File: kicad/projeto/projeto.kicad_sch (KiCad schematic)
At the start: 4 parts

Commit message: Iniciou o esquemático
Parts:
- removed Q?: BTA16-600B, Package_TO_SOT_THT:TO-220-3_Vertical, symbol Triac_Thyristor:BTA16-600B
- removed R? (x2): R, symbol Device:R
- removed Vca: VSIN, symbol Simulation_SPICE:VSIN
- added D01, D02, D03, D04, D?: UF5408, Diode_THT:D_DO-201AD_P15.24mm_Horizontal, symbol Diode:UF5408
- added D05: 5V, symbol Device:D_Zener
- added D?, Dss: LED, LED_THT:LED_D3.0mm, symbol Device:LED
- added J?: Conn_01x02_Male, Connector_PinHeader_2.54mm:PinHeader_1x02_P2.54mm_Vertical, symbol Connector:Conn_01x02_Male
- added Jac, Jl1, Jl2: Screw_Terminal_01x02, TerminalBlock:TerminalBlock_bornier-2_P5.08mm, symbol Connector:Screw_Terminal_01x02
- added Jdc: Barrel_Jack_MountingPin, Connector_BarrelJack:BarrelJack_Horizontal, symbol Connector:Barrel_Jack_MountingPin
- added Jsens: Screw_Terminal_01x06, TerminalBlock:TerminalBlock_bornier-6_P5.08mm, symbol Connector:Screw_Terminal_01x06
- added Q1, Q2: BTA16-600B, Package_TO_SOT_THT:TO-220-3_Vertical, symbol Triac_Thyristor:BTA16-600B
- added R01: 33k, Resistor_THT:R_Axial_DIN0207_L6.3mm_D2.5mm_P7.62mm_Horizontal, symbol Device:R
- added R02, Ren, Rexit, Rreset, Rsens1, Rsens2: 33K, Resistor_THT:R_Axial_DIN0207_L6.3mm_D2.5mm_P7.62mm_Horizontal, symbol Device:R
- added R?: R, Resistor_THT:R_Axial_DIN0207_L6.3mm_D2.5mm_P7.62mm_Horizontal, symbol Device:R
- added Rmoc1, Rmoc2: 150, Resistor_THT:R_Axial_DIN0207_L6.3mm_D2.5mm_P7.62mm_Horizontal, symbol Device:R
- added Rss: 260, Resistor_THT:R_Axial_DIN0207_L6.3mm_D2.5mm_P7.62mm_Horizontal, symbol Device:R
- added Rtriac1, Rtriac2: 180, Resistor_THT:R_Axial_DIN0309_L9.0mm_D3.2mm_P12.70mm_Horizontal, symbol Device:R
- added SWexit, SWreset: SW_Push, symbol Switch:SW_Push
- added U?: LM1117-3.3, symbol Regulator_Linear:LM1117-3.3
- added U?: ESP-12E, RF_Module:ESP-12E, symbol RF_Module:ESP-12E
- added Udet_0: 4N25, Package_DIP:DIP-6_W7.62mm, symbol Isolator:4N25
- added Uload1, Uload2: MOC3021M, symbol Relay_SolidState:MOC3021M
- added Umultiplex: CD4051B, Package_DIP:DIP-16_W7.62mm, symbol Analog_Switch:CD4051B
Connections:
- net GND: now also Dss.1 (K), Jdc.2, Rexit.2, Rsens2.2, SWreset.2, U?.1 (GND), Udet_0.4, Uload1.2, Uload2.2, Umultiplex.2 (X6), Umultiplex.4 (X7), Umultiplex.6 (INH), Umultiplex.7 (VEE), Umultiplex.8 (VSS)
- new net: D01.1 (K), D03.1 (K), D05.1 (K)
- new net: Rtriac1.1, Uload1.6
- new net: Jl1.2 (Pin_2), Q1.2 (A2), Rtriac1.2
- new net: Rmoc1.1, Uload1.1
- new net: Q1.3 (G), Uload1.4
- new net: D02.2 (A), D04.2 (A), Udet_0.2
- new net: Dss.2 (A), Rss.2
- new net: R01.2, Udet_0.1
- new net: Ren.1, U?.3 (EN)
- new net: D05.2 (A), R01.1
- new net: Rtriac2.1, Uload2.6
- new net: Jl2.2 (Pin_2), Q2.2 (A2), Rtriac2.2
- new net: Jsens.5 (Pin_5), Umultiplex.1 (X4)
- new net: Jsens.4 (Pin_4), Umultiplex.12 (X3)
- new net: Jsens.1 (Pin_1), Umultiplex.13 (X0)
- new net: Jsens.2 (Pin_2), Umultiplex.14 (X1)
- new net: Jsens.3 (Pin_3), Umultiplex.15 (X2)
- new net: Rsens1.1, Umultiplex.3 (X)
- new net: Jsens.6 (Pin_6), Umultiplex.5 (X5)
- new net: Rmoc2.1, Uload2.1
- new net: Q2.3 (G), Uload2.4
- new net +3V3: R02.1, Ren.2, Rreset.1, SWexit.1, U?.2 (VO), Umultiplex.16 (VDD)
- new net +5V: Jdc.1, U?.3 (VI)
- new net AC1: D01.2 (A), D02.1 (K), Jac.1 (Pin_1), Jl1.1 (Pin_1), Jl2.1 (Pin_1)
- new net AC2: D03.2 (A), D04.1 (K), Jac.2 (Pin_2), Q1.1 (A1), Q2.1 (A1)
- new net NC?: Jdc.MP (MountPin), Udet_0.6
- new net det_0_intr: R02.2, Udet_0.5
- new net drive_load_1: Rmoc1.2
- new net drive_load_2: Rmoc2.2
- new net exit_intr: Rexit.1, SWexit.2
- new net multiplex_A: U?.4 (GPIO16), Umultiplex.11 (A)
- new net multiplex_B: U?.5 (GPIO14), Umultiplex.10 (B)
- new net multiplex_C: U?.6 (GPIO12), Umultiplex.9 (C)
- new net multiplex_out: Rsens1.2, Rsens2.1, U?.2 (ADC)
- new net reset: Rreset.2, SWreset.1, U?.1 (~{RST})
- new net steady_state: Rss.1
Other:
- note added: "Buttons"
- note added: "COLOCAR A CONEXÃO DO 5V VINDO DO SERIAL AQUI"
- note added: "Load Driver"
- note added: "Power"
- note added: "Sensor"
- note added: "Steady State Status"
- note added: "Zero Detection"
- note removed: ".include D:\bolsa\controle_forno\circuitos\lib\moc302x.lib"
- note removed: ".tran 1u 0.05"

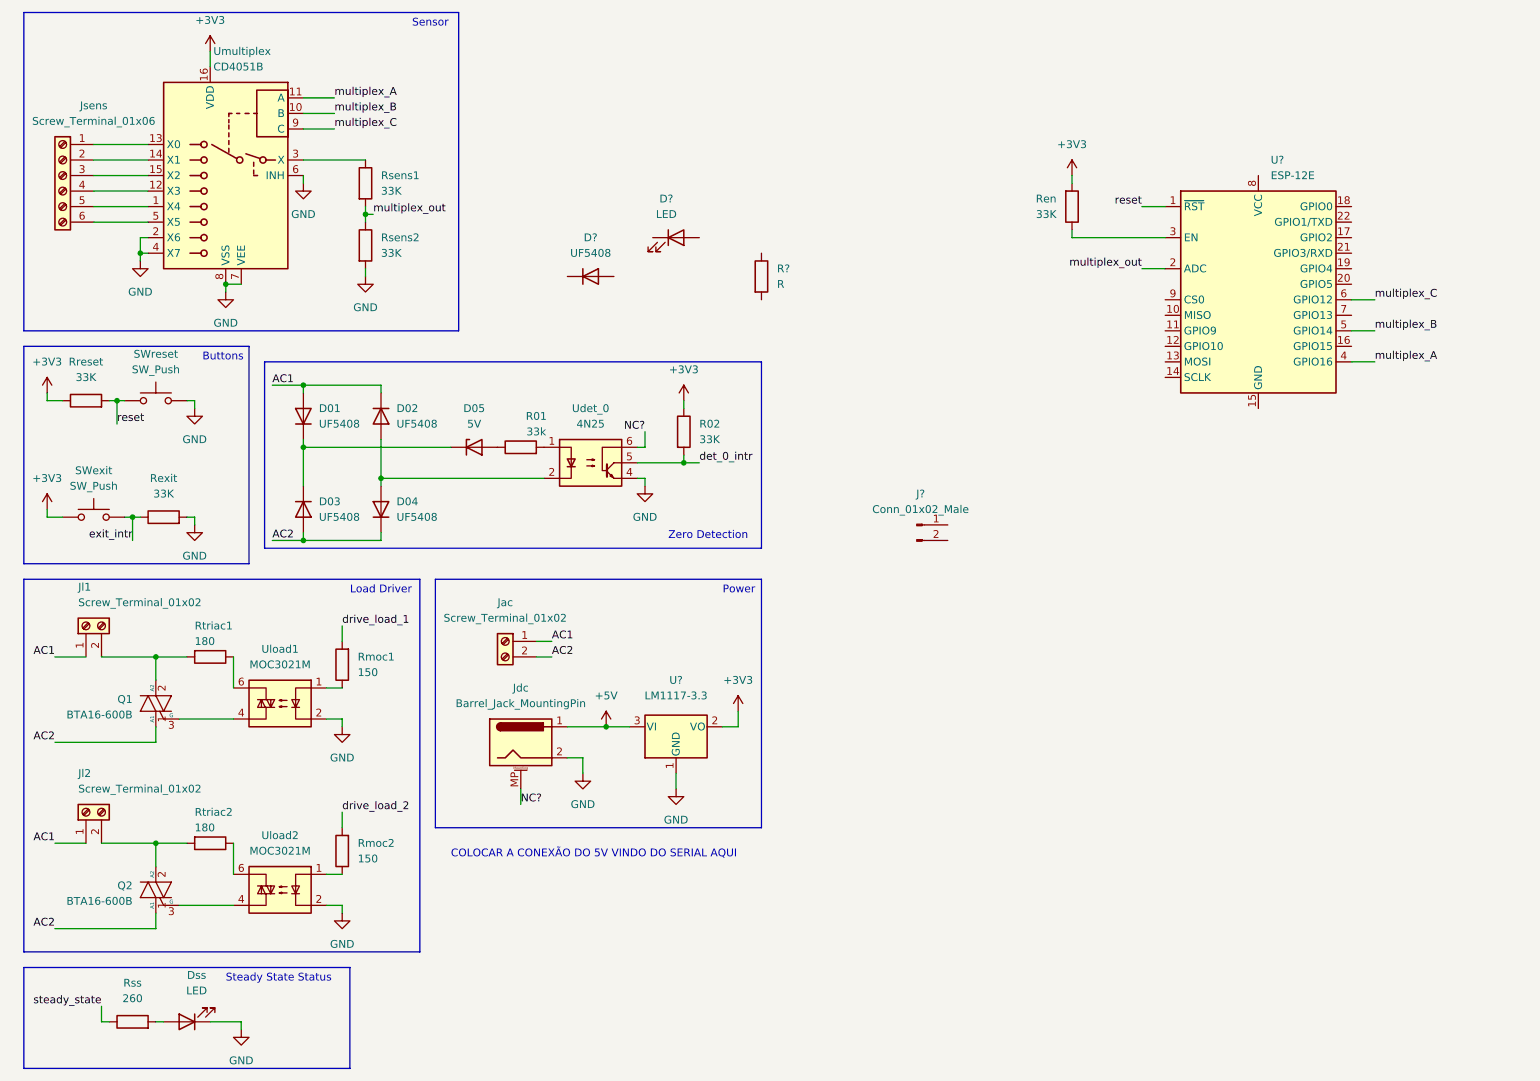
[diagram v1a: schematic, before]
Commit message: Finalizou esquematico
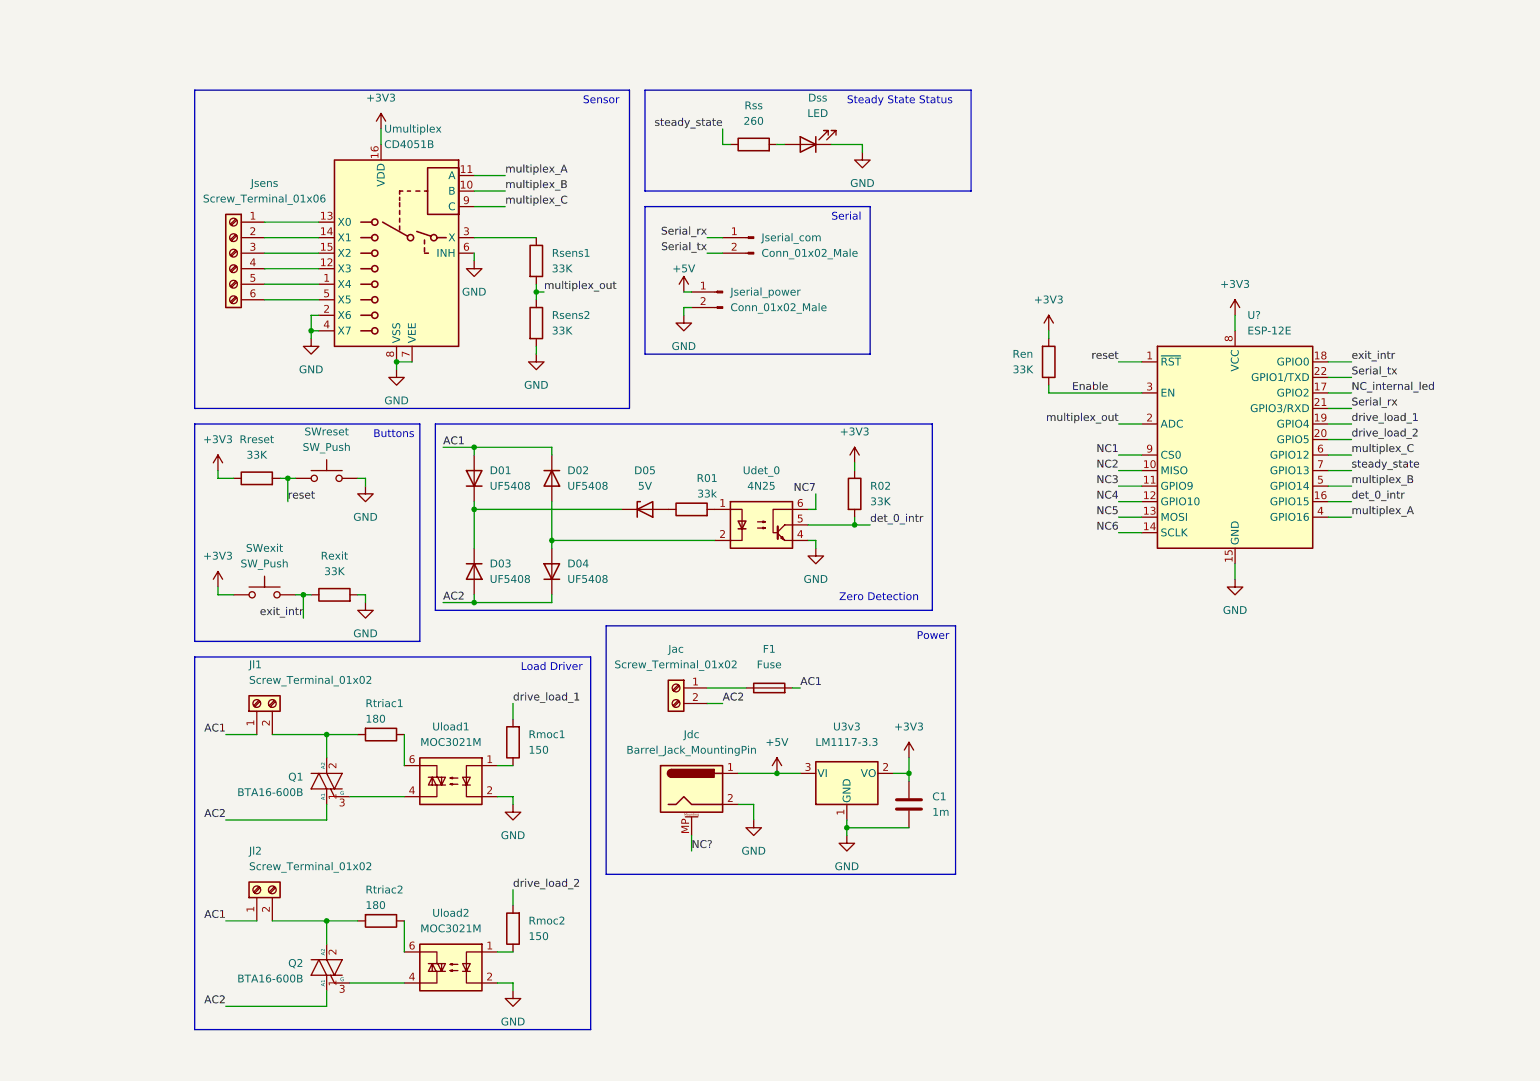
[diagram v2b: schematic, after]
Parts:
- removed D?: UF5408, Diode_THT:D_DO-201AD_P15.24mm_Horizontal, symbol Diode:UF5408
- removed D?: LED, LED_THT:LED_D3.0mm, symbol Device:LED
- removed J?: Conn_01x02_Male, Connector_PinHeader_2.54mm:PinHeader_1x02_P2.54mm_Vertical, symbol Connector:Conn_01x02_Male
- removed R?: R, Resistor_THT:R_Axial_DIN0207_L6.3mm_D2.5mm_P7.62mm_Horizontal, symbol Device:R
- added C1: 1m, symbol Device:C
- added F1: Fuse, Fuse:Fuseholder_Cylinder-5x20mm_Stelvio-Kontek_PTF78_Horizontal_Open, symbol Device:Fuse
- added Jserial_com, Jserial_power: Conn_01x02_Male, Connector_PinHeader_2.54mm:PinHeader_1x02_P2.54mm_Vertical, symbol Connector:Conn_01x02_Male
- U3v3: renamed from U?; footprint (none) -> Package_TO_SOT_THT:TO-220-3_Vertical
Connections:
- net +3V3: now also U?.8 (VCC), C1.1
- net +5V: now also Jserial_power.1 (Pin_1)
- net AC1: now also F1.2; no longer Jac.1 (Pin_1)
- net GND: now also U?.15 (GND), C1.2, Jserial_power.2 (Pin_2)
- net NC?: no longer Udet_0.6
- net det_0_intr: now also U?.16 (GPIO15)
- net drive_load_1: now also U?.19 (GPIO4)
- net drive_load_2: now also U?.20 (GPIO5)
- net exit_intr: now also U?.18 (GPIO0)
- net steady_state: now also U?.7 (GPIO13)
- net Enable: now reaches Ren.1, U?.3 (EN)
- net NC2: now reaches U?.10 (MISO)
- net NC3: now reaches U?.11 (GPIO9)
- net NC4: now reaches U?.12 (GPIO10)
- net NC5: now reaches U?.13 (MOSI)
- net NC6: now reaches U?.14 (SCLK)
- net NC_internal_led: now reaches U?.17 (GPIO2)
- net Serial_rx: now reaches U?.21 (GPIO3/RXD)
- net Serial_rx: now also Jserial_com.1 (Pin_1)
- net Serial_tx: now reaches U?.22 (GPIO1/TXD)
- net Serial_tx: now also Jserial_com.2 (Pin_2)
- net NC1: now reaches U?.9 (CS0)
- new net: F1.1, Jac.1 (Pin_1)
- new net NC7: Udet_0.6
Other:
- note added: "Serial"
- note removed: "COLOCAR A CONEXÃO DO 5V VINDO DO SERIAL AQUI"
- company: (none) -> LITel UFJF
- moved on the sheet: D01, D02, D03, D04, D05, Dss, Jac, Jdc, Jl1, Jl2, Jsens, Q1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

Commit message: Correção de erros do ERC
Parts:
- C1: footprint (none) -> Capacitor_THT:C_Radial_D10.0mm_H16.0mm_P5.00mm
- gave numbers to parts that had none: 1
- renumbered D01 to D1, D02 to D2, D03 to D3, D04 to D4, D05 to D5, Dss to Dss1, Jac to Jac1, Jdc to Jdc1, Jsens to Jsens1, Jserial_com to Jserial_com1, Jserial_power to Jserial_power1, R01 to R1, R02 to R2, Ren to Ren1, Rexit to Rexit1, Rreset to Rreset1, Rss to Rss1, SWexit to SWexit1, SWreset to SWreset1, Umultiplex to Umultiplex1
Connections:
- net GND: no longer Umultiplex1.2 (X6), Umultiplex1.4 (X7)
- net NC1: no longer names the net of U1.9 (CS0)
- net NC2: no longer names the net of U1.10 (MISO)
- net NC3: no longer names the net of U1.11 (GPIO9)
- net NC4: no longer names the net of U1.12 (GPIO10)
- net NC5: no longer names the net of U1.13 (MOSI)
- net NC6: no longer names the net of U1.14 (SCLK)
- net NC7: no longer names the net of Udet_0.6
- net NC?: no longer names the net of Jdc1.MP (MountPin)
- net NC_internal_led: no longer names the net of U1.17 (GPIO2)
- no-connect marks 0 -> 11
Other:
- note added: "NC_internal_led"
- moved on the sheet: C1, U3v3

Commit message: Att componentes
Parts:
- removed Jsens1: Screw_Terminal_01x06, TerminalBlock:TerminalBlock_bornier-6_P5.08mm, symbol Connector:Screw_Terminal_01x06
- added Jpwr_sens1, Jpwr_sens2, Jsens1: Conn_01x08_Male, Connector_PinHeader_2.54mm:PinHeader_1x08_P2.54mm_Vertical, symbol Connector:Conn_01x08_Male
- Rexit1, Rreset1, Rsens1, Rsens2: value 33K -> 10K
- Rmoc1, Rmoc2: value 150 -> 240
- Rz1: renamed from R1; footprint Resistor_THT:R_Axial_DIN0207_L6.3mm_D2.5mm_P7.62mm_Horizontal -> Resistor_THT:R_Axial_DIN0207_L6.3mm_D2.5mm_P10.16mm_Horizontal
- SWexit1, SWreset1: footprint (none) -> Button_Switch_THT:SW_PUSH_6mm
- Uload1, Uload2: value MOC3021M -> MOC3023M; footprint (none) -> Package_DIP:DIP-6_W7.62mm_Socket
- Umultiplex1: footprint Package_DIP:DIP-16_W7.62mm -> Package_DIP:DIP-16_W7.62mm_Socket
- renumbered R2 to Rz2
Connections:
- net +5V: now also Jpwr_sens1.1 (Pin_1), Jpwr_sens1.2 (Pin_2), Jpwr_sens1.3 (Pin_3), Jpwr_sens1.4 (Pin_4), Jpwr_sens1.5 (Pin_5), Jpwr_sens1.6 (Pin_6), Jpwr_sens1.7 (Pin_7), Jpwr_sens1.8 (Pin_8)
- net GND: now also Jpwr_sens2.1 (Pin_1), Jpwr_sens2.2 (Pin_2), Jpwr_sens2.3 (Pin_3), Jpwr_sens2.4 (Pin_4), Jpwr_sens2.5 (Pin_5), Jpwr_sens2.6 (Pin_6), Jpwr_sens2.7 (Pin_7), Jpwr_sens2.8 (Pin_8)
- net at Umultiplex1.1 (X4): now also Jsens1.5 (Pin_5)
- net at Umultiplex1.12 (X3): now also Jsens1.4 (Pin_4)
- net at Umultiplex1.13 (X0): now also Jsens1.1 (Pin_1)
- net at Umultiplex1.14 (X1): now also Jsens1.2 (Pin_2)
- net at Umultiplex1.15 (X2): now also Jsens1.3 (Pin_3)
- net at Umultiplex1.2 (X6): now also Jsens1.7 (Pin_7)
- net at Umultiplex1.4 (X7): now also Jsens1.8 (Pin_8)
- net at Umultiplex1.5 (X5): now also Jsens1.6 (Pin_6)
- no-connect marks 11 -> 9
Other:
- moved on the sheet: Ren1, U1

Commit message: Att componentes
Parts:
- added C1: 1m, Capacitor_THT:C_Radial_D10.0mm_H16.0mm_P5.00mm, symbol Device:C
- renumbered C1 to C2
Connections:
- net +5V: now also C1.1
- net GND: now also C1.2
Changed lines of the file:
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@@
   (junction (at 60.96 110.49) (diameter 0) (color 0 0 0 0)
   )
-  (junction (at 134.62 144.78) (diameter 0) (color 0 0 0 0)
-  )
   (junction (at 210.82 138.43) (diameter 0) (color 0 0 0 0)
   )
@@
   (junction (at 199.39 133.35) (diameter 0) (color 0 0 0 0)
   )
+  (junction (at 138.43 147.32) (diameter 0) (color 0 0 0 0)
+  )
   (junction (at 58.42 91.44) (diameter 0) (color 0 0 0 0)
   )
@@
   )
   (junction (at 64.77 133.35) (diameter 0) (color 0 0 0 0)
+  )
+  (junction (at 134.62 147.32) (diameter 0) (color 0 0 0 0)
+  )
+  (junction (at 138.43 139.7) (diameter 0) (color 0 0 0 0)
   )
   (junction (at 152.4 139.7) (diameter 0) (color 0 0 0 0)
@@
   (no_connect (at 144.78 96.52))
   (no_connect (at 241.3 58.42))
+  (wire (pts (xy 165.1 148.59) (xy 175.26 148.59))
+    (stroke (width 0) (type default) (color 0 0 0 0))
+  )
   (wire (pts (xy 64.77 144.78) (xy 64.77 147.32))
     (stroke (width 0) (type default) (color 0 0 0 0))
@@
     (stroke (width 0) (type default) (color 0 0 0 0))
   )
+  (wire (pts (xy 138.43 139.7) (xy 152.4 139.7))
+    (stroke (width 0) (type default) (color 0 0 0 0))
+  )
   (wire (pts (xy 127 52.07) (xy 129.54 52.07))
     (stroke (width 0) (type default) (color 0 0 0 0))
@@
     (stroke (width 0) (type default) (color 0 0 0 0))
   )
+  (wire (pts (xy 134.62 147.32) (xy 138.43 147.32))
+    (stroke (width 0) (type default) (color 0 0 0 0))
+  )
   (wire (pts (xy 207.01 73.66) (xy 203.2 73.66))
     (stroke (width 0) (type default) (color 0 0 0 0))
@@
     (stroke (width 0) (type default) (color 0 0 0 0))
   )
-  (wire (pts (xy 132.08 139.7) (xy 152.4 139.7))
+  (wire (pts (xy 132.08 139.7) (xy 138.43 139.7))
     (stroke (width 0) (type default) (color 0 0 0 0))
   )
@@
   )
   (wire (pts (xy 140.97 125.73) (xy 142.24 125.73))
-    (stroke (width 0) (type default) (color 0 0 0 0))
-  )
-  (wire (pts (xy 165.1 148.59) (xy 175.26 148.59))
     (stroke (width 0) (type default) (color 0 0 0 0))
   )
@@
   )
   (symbol (lib_id "power:GND") (at 134.62 147.32 0) (unit 1)
-    (in_bom yes) (on_board yes) (fields_autoplaced)
+    (in_bom yes) (on_board yes)
     (property "Reference" "#PWR0108" (id 0) (at 134.62 153.67 0)
       (effects (font (size 1.27 1.27)) hide)
     )
-    (property "Value" "GND" (id 1) (at 134.62 152.4 0))
+    (property "Value" "GND" (id 1) (at 132.08 151.13 0))
     (property "Footprint" "" (id 2) (at 134.62 147.32 0)
       (effects (font (size 1.27 1.27)) hide)
@@
     )
     (property "Datasheet" "~" (id 3) (at 73.66 163.83 0)
+      (effects (font (size 1.27 1.27)) hide)
+    )
+    (pin "1")
+    (pin "2")
+  )
+  (symbol (lib_id "Device:C") (at 138.43 143.51 0) (unit 1)
+    (in_bom yes) (on_board yes) (fields_autoplaced)
+    (property "Reference" "C1" (id 0) (at 142.24 142.2399 0)
+      (effects (font (size 1.27 1.27)) (justify left))
+    )
+    (property "Value" "1m" (id 1) (at 142.24 144.7799 0)
+      (effects (font (size 1.27 1.27)) (justify left))
+    )
+    (property "Footprint" "Capacitor_THT:C_Radial_D10.0mm_H16.0mm_P5.00mm" (id 2) (at 139.3952 147.32 0)
+      (effects (font (size 1.27 1.27)) hide)
+    )
+    (property "Datasheet" "~" (id 3) (at 138.43 143.51 0)
       (effects (font (size 1.27 1.27)) hide)
     )
@@
   (symbol (lib_id "Device:C") (at 175.26 144.78 0) (unit 1)
     (in_bom yes) (on_board yes) (fields_autoplaced)
-    (property "Reference" "C1" (id 0) (at 179.07 143.5099 0)
+    (property "Reference" "C2" (id 0) (at 179.07 143.5099 0)
       (effects (font (size 1.27 1.27)) (justify left))
     )
@@
     (pin "2")
   )
-  (symbol (lib_id "power:PWR_FLAG") (at 134.62 144.78 0) (unit 1)
-    (in_bom yes) (on_board yes) (fields_autoplaced)
-    (property "Reference" "#FLG0101" (id 0) (at 134.62 142.875 0)
-      (effects (font (size 1.27 1.27)) hide)
-    )
-    (property "Value" "PWR_FLAG" (id 1) (at 137.16 143.5099 0)
-      (effects (font (size 1.27 1.27)) (justify left))
-    )
-    (property "Footprint" "" (id 2) (at 134.62 144.78 0)
-      (effects (font (size 1.27 1.27)) hide)
-    )
-    (property "Datasheet" "~" (id 3) (at 134.62 144.78 0)
+  (symbol (lib_id "power:PWR_FLAG") (at 138.43 147.32 180) (unit 1)
+    (in_bom yes) (on_board yes)
+    (property "Reference" "#FLG0101" (id 0) (at 138.43 149.225 0)
+      (effects (font (size 1.27 1.27)) hide)
+    )
+    (property "Value" "PWR_FLAG" (id 1) (at 147.32 151.13 0)
+      (effects (font (size 1.27 1.27)) (justify left))
+    )
+    (property "Footprint" "" (id 2) (at 138.43 147.32 0)
+      (effects (font (size 1.27 1.27)) hide)
+    )
+    (property "Datasheet" "~" (id 3) (at 138.43 147.32 0)
       (effects (font (size 1.27 1.27)) hide)
     )
@@
       (reference "#PWR0124") (unit 1) (value "GND") (footprint "")
     )
+    (path "/80ebf0af-a71f-42a9-abab-839fb7cffa2d"
+      (reference "C1") (unit 1) (value "1m") (footprint "Capacitor_THT:C_Radial_D10.0mm_H16.0mm_P5.00mm")
+    )
     (path "/da3a6a44-7c4e-4b57-b3f7-f3c72ed95869"
-      (reference "C1") (unit 1) (value "1m") (footprint "Capacitor_THT:C_Radial_D10.0mm_H16.0mm_P5.00mm")
+      (reference "C2") (unit 1) (value "1m") (footprint "Capacitor_THT:C_Radial_D10.0mm_H16.0mm_P5.00mm")
     )
     (path "/6c7ba7e5-1a29-4616-9eaf-31ecc6a51cb4"
